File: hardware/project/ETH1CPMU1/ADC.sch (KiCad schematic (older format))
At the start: 0 parts

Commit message: Schematic design
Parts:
- added U1001, U1002, U1003, U1004: INA159, symbol ETH1CPMU1:INA159
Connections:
- new net: U1001.5 (SENS), U1001.6 (OUT)
- new net: U1002.5 (SENS), U1002.6 (OUT)
- new net: U1003.5 (SENS), U1003.6 (OUT)
- new net: U1004.5 (SENS), U1004.6 (OUT)
- new net +5VF: U1001.7 (V+), U1002.7 (V+), U1003.7 (V+), U1004.7 (V+)
- new net AGNDF: U1001.1 (REF1), U1001.2 (-IN), U1001.4 (V-), U1002.1 (REF1), U1002.2 (-IN), U1002.4 (V-), U1003.1 (REF1), U1003.2 (-IN), U1003.4 (V-), U1004.1 (REF1), U1004.2 (-IN), U1004.4 (V-)

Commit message: Schematic design
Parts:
- added C1001, C1002, C1003, C1004: 1n, symbol Device:C
- added R1001, R1002, R1003, R1004: 100, symbol Device:R
- added U1005: ADS8363, symbol ETH1CPMU1:ADS8363
- added U1404: ADG1414BRU, Package_SO:TSSOP-24_4.4x7.8mm_P0.65mm, symbol Analog_Switch:ADG1414BRU
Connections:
- net labels added: +15VF, +3.3VF, -15VF, AC_FOURCE, ADC_BUSY, ADC_CLOCK, ADC_MUX_DIN, ADC_MUX_SCLK, ADC_MUX_SDO, ADC_MUX_~SYNC, ADC_RD, ADC_SDI, ADC_SDOA, ADC_~CS, DC_FOURCE, DGNDF, PMU_MEASIOUT, PMU_MEASVOUT
- wire segments 20 -> 123
- no-connect marks 0 -> 5
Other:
- moved on the sheet: U1001, U1002, U1003, U1004

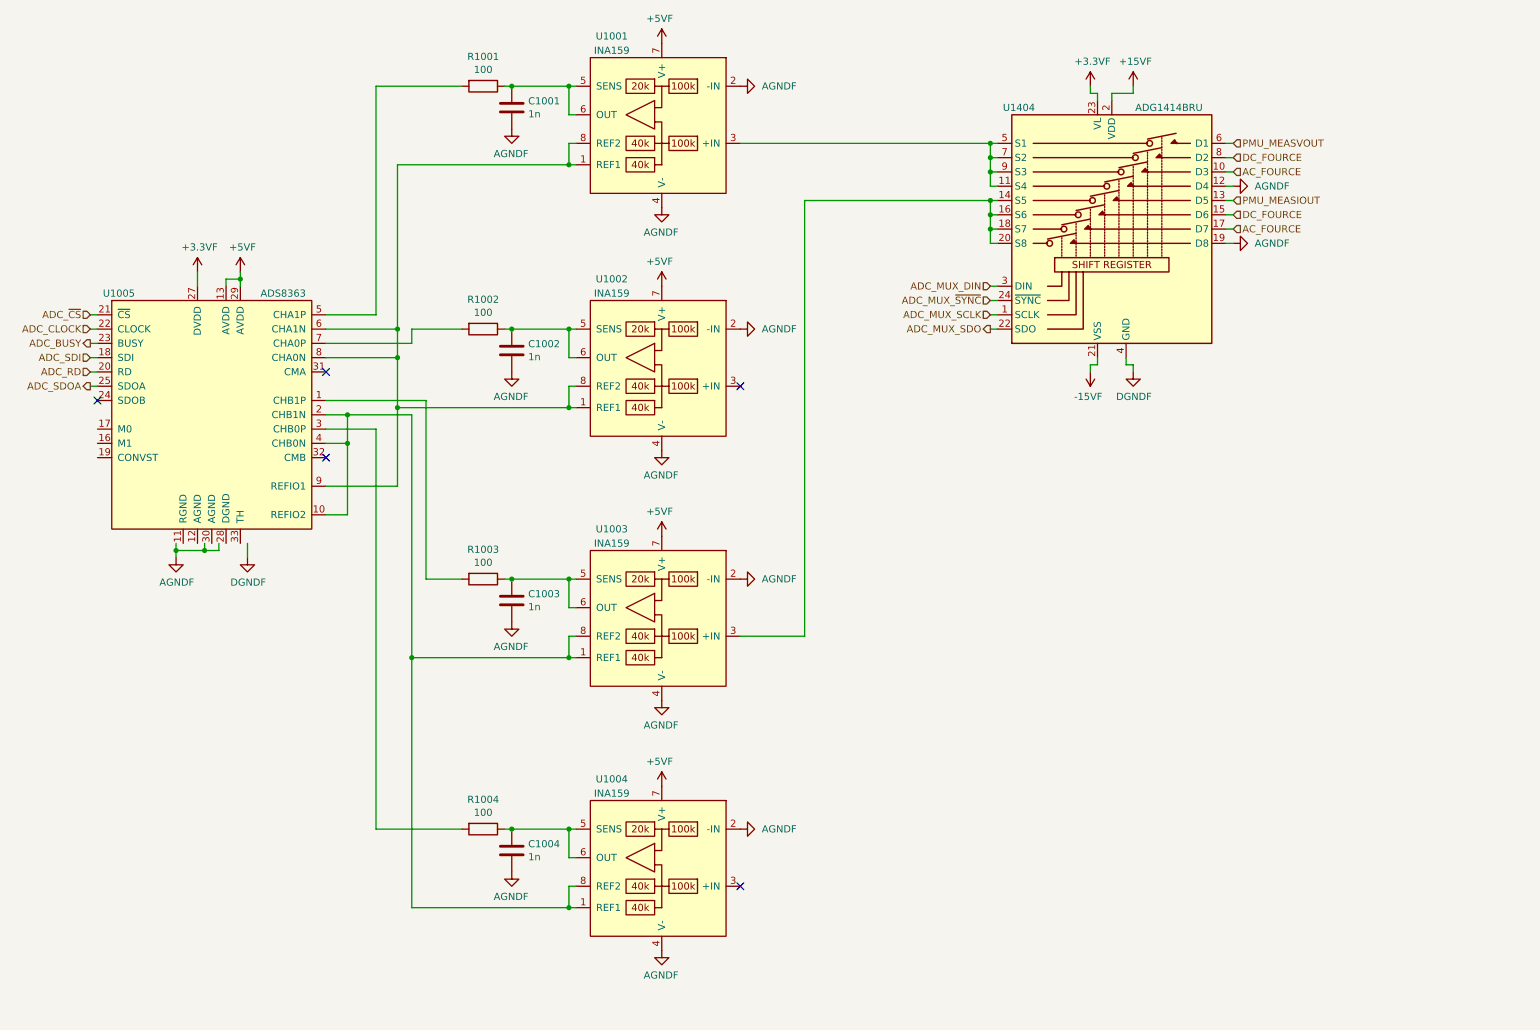
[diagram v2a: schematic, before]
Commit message: Function generator schematic design.
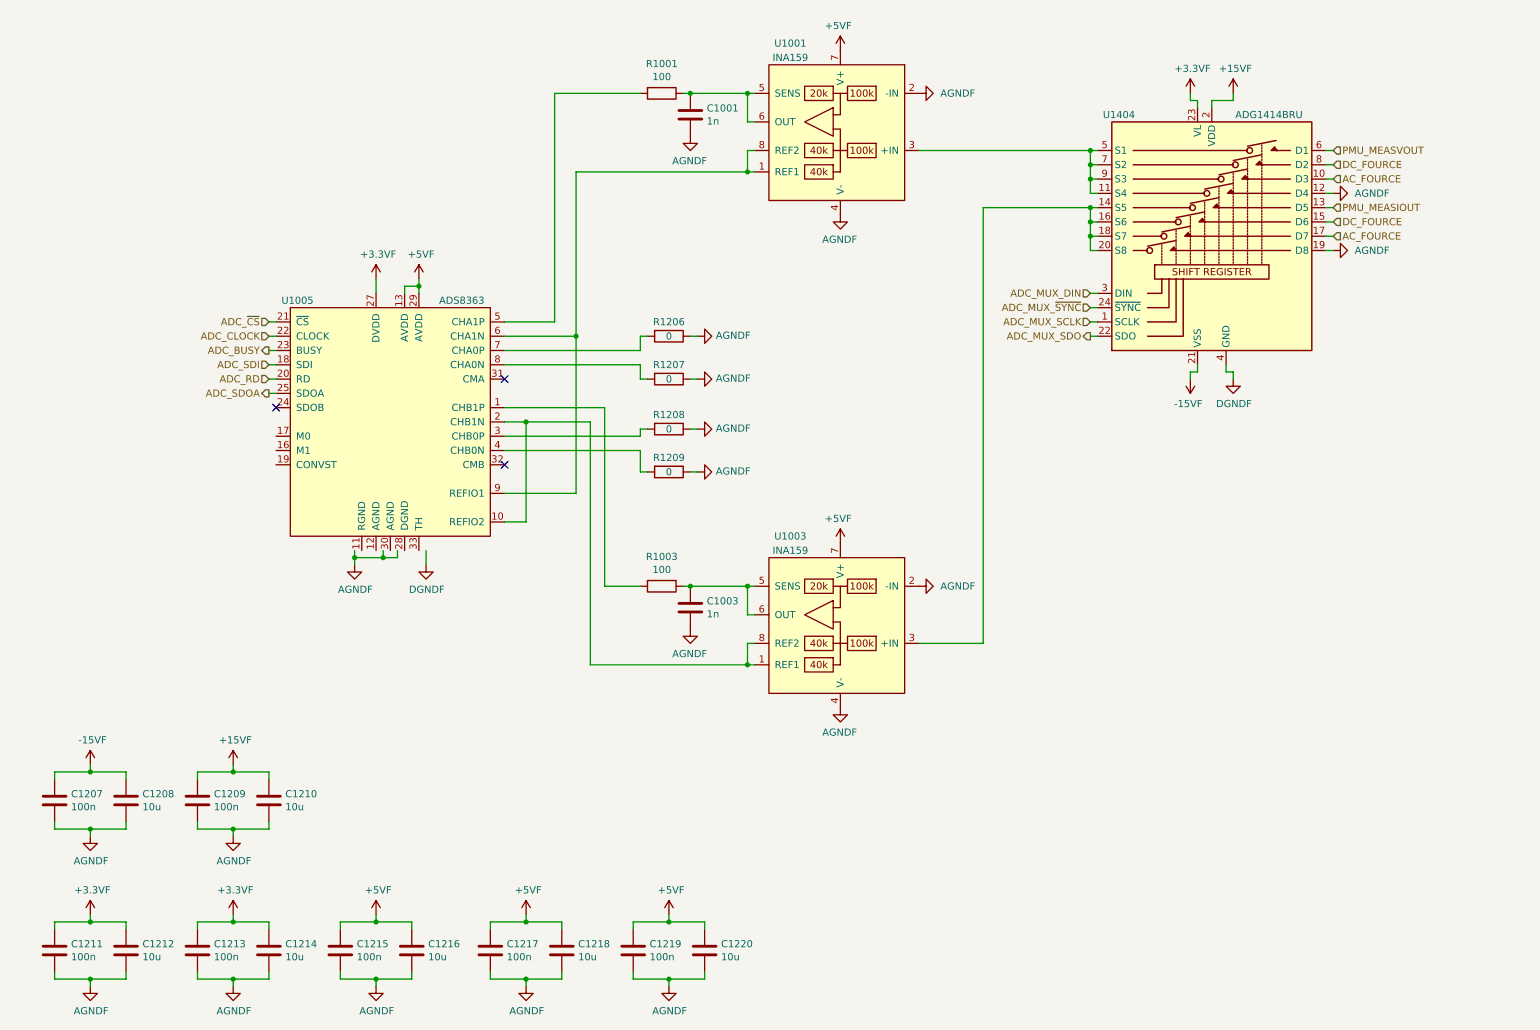
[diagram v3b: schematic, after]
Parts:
- removed C1002, C1004: 1n, symbol Device:C
- removed R1002, R1004: 100, symbol Device:R
- removed U1002, U1004: INA159, symbol ETH1CPMU1:INA159
- added C1207, C1209, C1211, C1213, C1215, C1217, C1219: 100n, Capacitor_SMD:C_0603_1608Metric_Pad1.05x0.95mm_HandSolder, symbol Device:C
- added C1208, C1210, C1212, C1214, C1216, C1218, C1220: 10u, Capacitor_SMD:C_1206_3216Metric_Pad1.42x1.75mm_HandSolder, symbol Device:C
- added R1206, R1207, R1208, R1209: 0, Resistor_SMD:R_0603_1608Metric_Pad1.05x0.95mm_HandSolder, symbol Device:R
- C1001, C1003: footprint (none) -> Capacitor_SMD:C_0603_1608Metric_Pad1.05x0.95mm_HandSolder
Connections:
- wire segments 123 -> 179
- no-connect marks 5 -> 3
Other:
- moved on the sheet: C1001, C1003, R1001, R1003, U1001, U1003, U1005, U1404

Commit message: Function generator schematic development.
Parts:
- R1001, R1003: footprint (none) -> Resistor_SMD:R_0603_1608Metric_Pad1.05x0.95mm_HandSolder
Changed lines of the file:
@@
 EESchema Schematic File Version 4
-LIBS:ETH1CPMU1-cache
 EELAYER 30 0
 EELAYER END
@@
 F 0 "R1001" V 4843 1150 50  0000 C CNN
 F 1 "100" V 4934 1150 50  0000 C CNN
-F 2 "" V 4980 1150 50  0001 C CNN
+F 2 "Resistor_SMD:R_0603_1608Metric_Pad1.05x0.95mm_HandSolder" V 4980 1150 50  0001 C CNN
 F 3 "~" H 5050 1150 50  0001 C CNN
 	1    5050 1150
@@
 F 0 "R1003" V 4843 4600 50  0000 C CNN
 F 1 "100" V 4934 4600 50  0000 C CNN
-F 2 "" V 4980 4600 50  0001 C CNN
+F 2 "Resistor_SMD:R_0603_1608Metric_Pad1.05x0.95mm_HandSolder" V 4980 4600 50  0001 C CNN
 F 3 "~" H 5050 4600 50  0001 C CNN
 	1    5050 4600

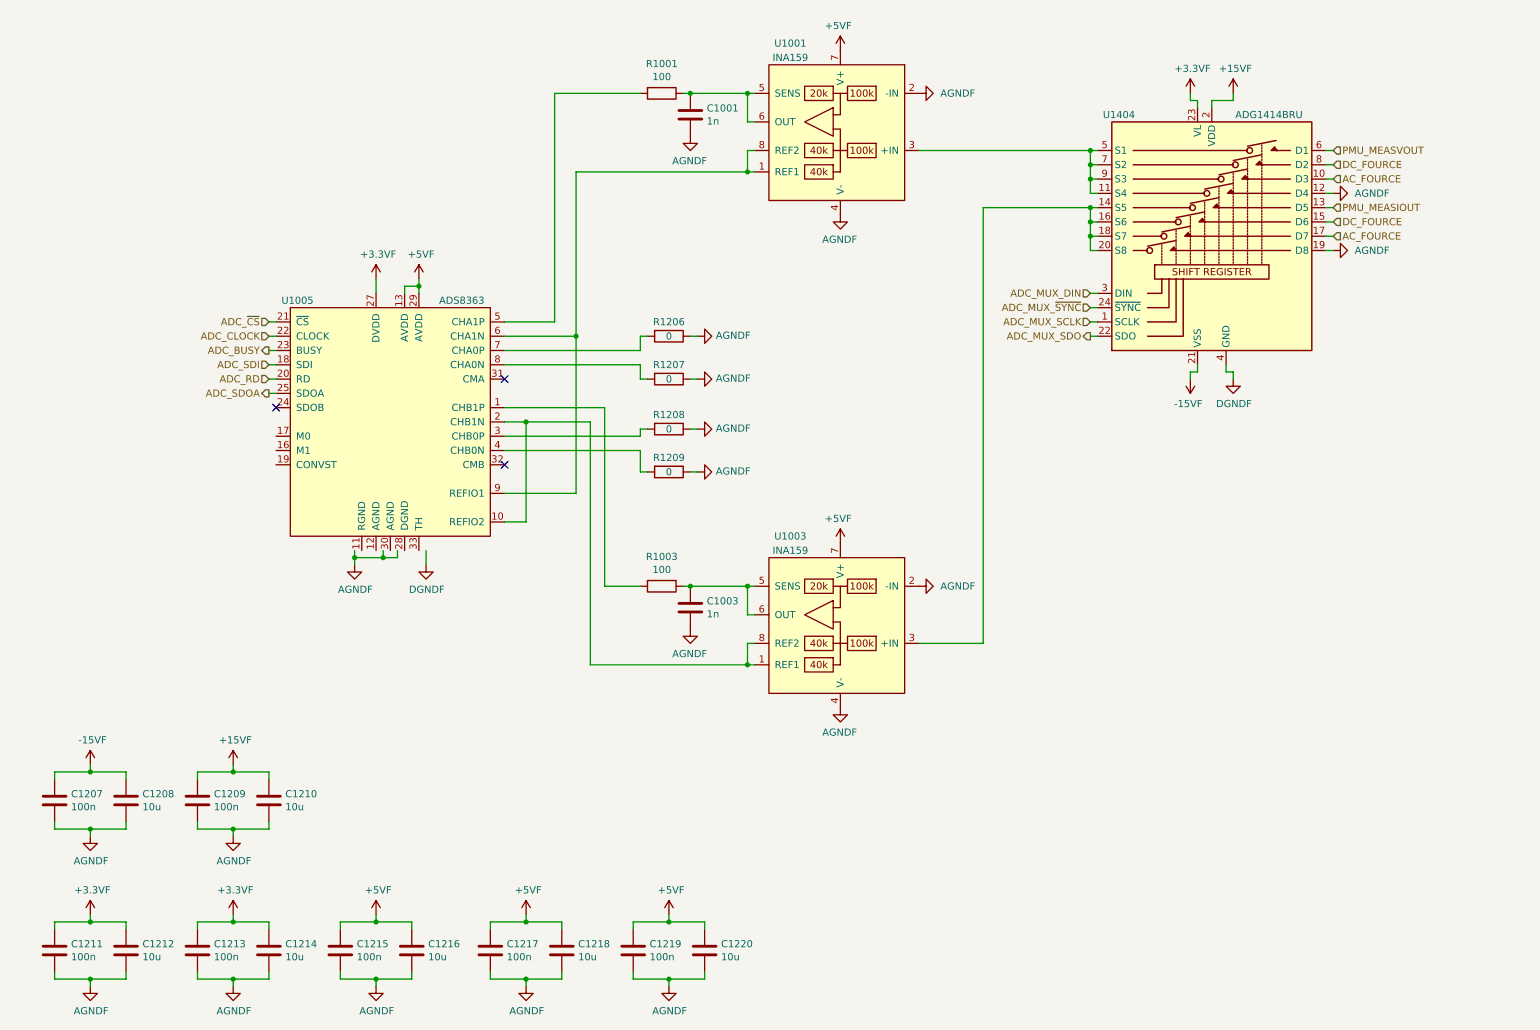
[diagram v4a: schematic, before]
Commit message: New footprint development, changes in schematics.
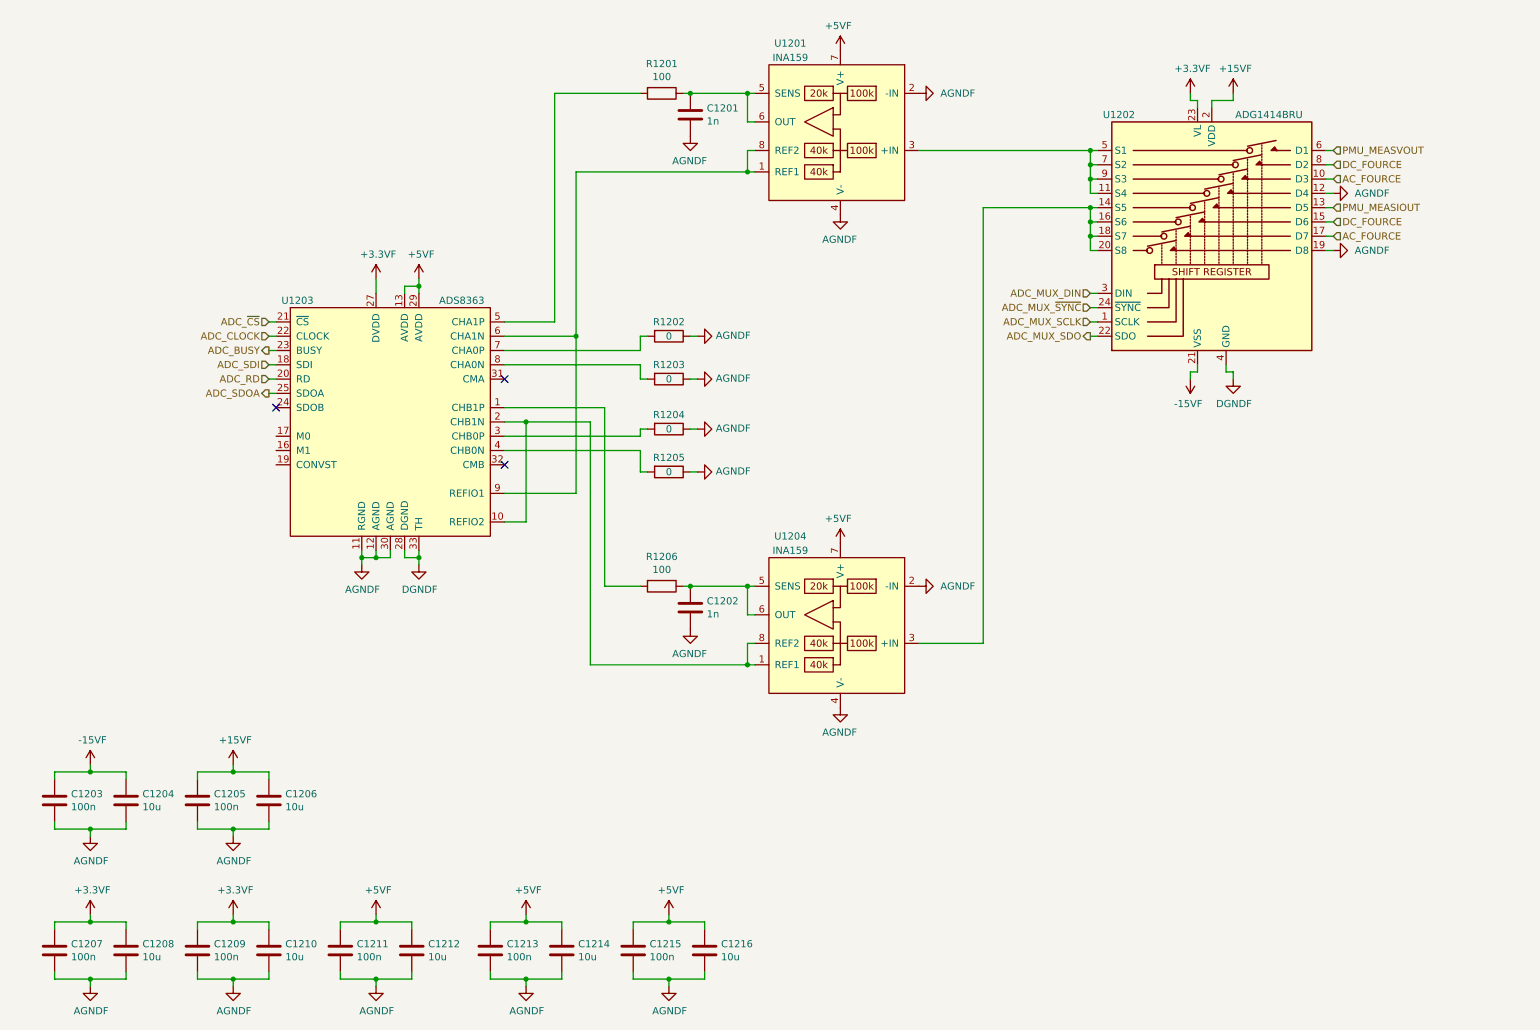
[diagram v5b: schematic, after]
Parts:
- U1201: renamed from U1001; footprint (none) -> Package_SO:MSOP-8_3x3mm_P0.65mm
- U1203: renamed from U1005; footprint (none) -> Package_DFN_QFN:QFN-32-1EP_5x5mm_P0.5mm_EP3.6x3.6mm_ThermalVias
- U1204: renamed from U1003; footprint (none) -> Package_SO:MSOP-8_3x3mm_P0.65mm
- renumbered C1001 to C1201, C1003 to C1202, C1207 to C1203, C1208 to C1204, C1209 to C1205, C1210 to C1206, C1211 to C1207, C1212 to C1208, C1213 to C1209, C1214 to C1210, C1215 to C1211, C1216 to C1212, C1217 to C1213, C1218 to C1214, C1219 to C1215, C1220 to C1216, R1001 to R1201, R1206 to R1202, R1207 to R1203, R1208 to R1204, R1209 to R1205, R1003 to R1206, U1404 to U1202
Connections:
- net AGNDF: now also U1203.11 (RGND), U1203.12 (AGND), U1203.30 (AGND)
- net DGNDF: now also U1203.28 (DGND), U1203.33 (TH)

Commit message: Schematic design
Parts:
- removed R1202, R1203: 0, Resistor_SMD:R_0603_1608Metric_Pad1.05x0.95mm_HandSolder, symbol Device:R
- added C902: 1n, Capacitor_SMD:C_0603_1608Metric_Pad1.05x0.95mm_HandSolder, symbol Device:C
- added R902: 100, Resistor_SMD:R_0603_1608Metric_Pad1.05x0.95mm_HandSolder, symbol Device:R
- added U903: INA159, Package_SO:MSOP-8_3x3mm_P0.65mm, symbol ETH1CPMU1:INA159
- renumbered C1201 to C901, C1202 to C903, C1203 to C904, C1204 to C905, C1205 to C906, C1206 to C907, C1207 to C908, C1208 to C909, C1209 to C910, C1210 to C911, C1211 to C912, C1212 to C913, C1213 to C914, C1214 to C915, C1215 to C916, C1216 to C917, R1201 to R901, R1204 to R903, R1205 to R904, R1206 to R905, U1201 to U901, U1202 to U902, U1203 to U904, U1204 to U905
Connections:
- net +5VF: now also U903.7 (V+)
- net AGNDF: now also C902.2, U903.2 (-IN), U903.4 (V-)
- net at U901.1 (REF1), U901.8 (REF2), U904.6 (CHA1N)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: now also U904.8 (CHA0N), U903.1 (REF1), U903.8 (REF2)
- net at U904.7 (CHA0P): now also R902.2
- new net: C902.1, R902.1, U903.5 (SENS), U903.6 (OUT)
- new net PMU_MEASOUT: U903.3 (+IN)
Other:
- moved on the sheet: R903, R904, U902

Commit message: PCB design.
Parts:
- C905, C907, C909, C911, C913, C915, C917: footprint Capacitor_SMD:C_1206_3216Metric_Pad1.42x1.75mm_HandSolder -> Capacitor_SMD:C_0805_2012Metric_Pad1.15x1.40mm_HandSolder
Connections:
- net +3.3VF: now also U904.16 (M1)
- net DGNDF: now also U904.17 (M0)
- net ADC_CONVST: now reaches U904.19 (CONVST)

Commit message: PCB design
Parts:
- added R906, R907: 0, Resistor_SMD:R_0603_1608Metric_Pad1.05x0.95mm_HandSolder, symbol Device:R
- renumbered C904 to C901, C908 to C902, C905 to C903, C909 to C904, C906 to C905, C910 to C906, C911 to C908, C912 to C909, C913 to C910, C914 to C911, C915 to C912, C916 to C913, C901 to C914, C902 to C915, C903 to C916, R905 to R903, R903 to R904, R904 to R905, U904 to U901, U901 to U902, U905 to U904, U902 to U905
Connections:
- net at U902.3 (+IN), U905.11 (S4), U905.5 (S1)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: now also R906.1
- net at U904.3 (+IN), U905.14 (S5), U905.16 (S6)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: now also R907.2
- net PMU_MEASIOUT renamed PMU_MEASI_GAIN
- net PMU_MEASI_GAIN: now also R907.1
- net PMU_MEASOUT renamed PMU_MEAS_GAIN
- net PMU_MEASVOUT renamed PMU_MEASV_GAIN
- net PMU_MEASV_GAIN: now also R906.2
